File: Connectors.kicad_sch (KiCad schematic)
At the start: 13 parts, among them J2 ZX-PZ2.54-1-5PZZ, J3 Conn_01x03_Socket, U7 TJA1051T/3

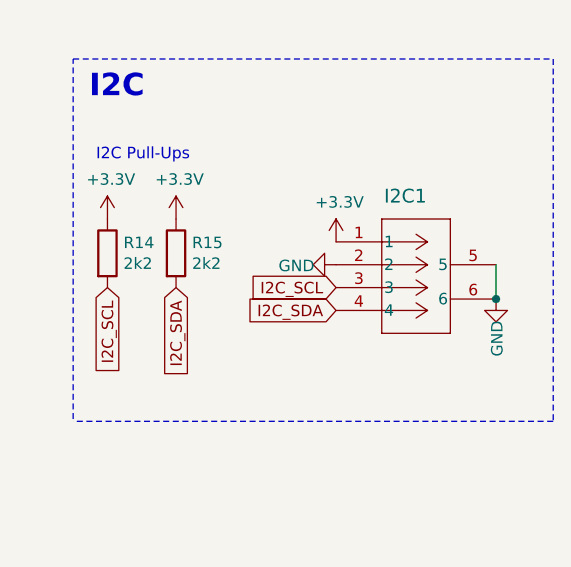
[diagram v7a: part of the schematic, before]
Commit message: IMU_IMU V1.0 is ready.
correct ch340e
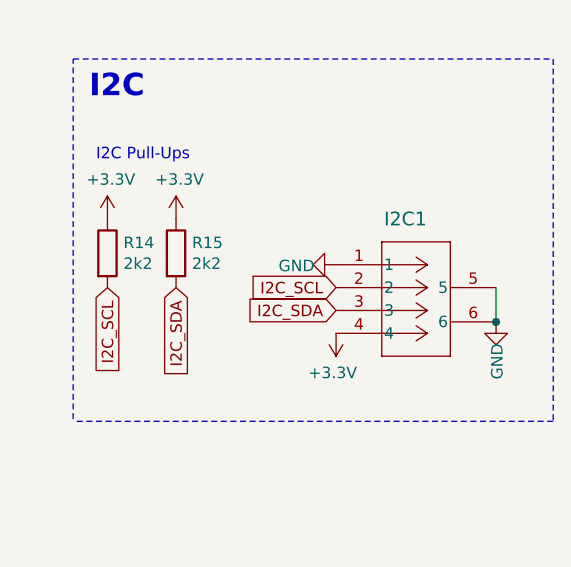
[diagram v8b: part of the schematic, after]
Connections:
- net +3.3V: now also I2C1.4; no longer I2C1.1
- net GND: now also I2C1.1; no longer I2C1.2
- net I2C_SCL: now also I2C1.2; no longer I2C1.3
- net I2C_SDA: now also I2C1.3; no longer I2C1.4
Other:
- moved on the sheet: I2C1
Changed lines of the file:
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@@
-	)
-	(junction
-		(at 218.44 67.31)
-		(diameter 0)
-		(color 0 0 0 0)
 	)
 	(junction
@@
 		(color 0 0 0 0)
 	)
+	(junction
+		(at 218.44 69.85)
+		(diameter 0)
+		(color 0 0 0 0)
+	)
 	(wire
 		(pts
@@
 		)
 	)
+	(polyline
+		(pts
+			(xy 224.79 40.64) (xy 224.79 80.899)
+		)
+		(stroke
+			(width 0)
+			(type dash)
+		)
+	)
 	(wire
 		(pts
@@
 		)
 	)
-	(wire
-		(pts
-			(xy 218.44 63.5) (xy 218.44 67.31)
-		)
-		(stroke
-			(width 0)
-			(type default)
-		)
-	)
 	(polyline
 		(pts
-			(xy 224.79 40.64) (xy 224.79 80.899)
+			(xy 224.79 80.899) (xy 171.45 80.899)
 		)
 		(stroke
@@
 	(polyline
 		(pts
-			(xy 224.79 80.899) (xy 171.45 80.899)
+			(xy 34.29 96.52) (xy 34.29 25.4)
 		)
 		(stroke
@@
 	(polyline
 		(pts
-			(xy 34.29 96.52) (xy 34.29 25.4)
+			(xy 88.9 165.989) (xy 35.56 165.989)
 		)
 		(stroke
@@
 		)
 	)
+	(wire
+		(pts
+			(xy 95.25 63.5) (xy 101.6 63.5)
+		)
+		(stroke
+			(width 0)
+			(type default)
+		)
+	)
 	(polyline
 		(pts
-			(xy 88.9 165.989) (xy 35.56 165.989)
+			(xy 171.45 80.645) (xy 171.45 40.64)
 		)
 		(stroke
@@
 	(wire
 		(pts
-			(xy 95.25 63.5) (xy 101.6 63.5)
+			(xy 60.96 138.43) (xy 62.23 138.43)
+		)
+		(stroke
+			(width 0)
+			(type default)
+		)
+	)
+	(wire
+		(pts
+			(xy 67.31 138.43) (xy 69.85 138.43)
+		)
+		(stroke
+			(width 0)
+			(type default)
+		)
+	)
+	(wire
+		(pts
+			(xy 101.6 68.58) (xy 109.22 68.58)
+		)
+		(stroke
+			(width 0)
+			(type default)
+		)
+	)
+	(wire
+		(pts
+			(xy 109.22 66.04) (xy 85.09 66.04)
+		)
+		(stroke
+			(width 0)
+			(type default)
+		)
+	)
+	(wire
+		(pts
+			(xy 101.6 63.5) (xy 101.6 68.58)
 		)
 		(stroke
@@
 	(polyline
 		(pts
-			(xy 171.45 80.645) (xy 171.45 40.64)
+			(xy 34.29 24.1301) (xy 138.43 24.1301)
 		)
 		(stroke
@@
 	(wire
 		(pts
-			(xy 60.96 138.43) (xy 62.23 138.43)
-		)
-		(stroke
-			(width 0)
-			(type default)
-		)
-	)
-	(wire
-		(pts
-			(xy 67.31 138.43) (xy 69.85 138.43)
-		)
-		(stroke
-			(width 0)
-			(type default)
-		)
-	)
-	(wire
-		(pts
-			(xy 101.6 68.58) (xy 109.22 68.58)
-		)
-		(stroke
-			(width 0)
-			(type default)
-		)
-	)
-	(wire
-		(pts
-			(xy 109.22 66.04) (xy 85.09 66.04)
-		)
-		(stroke
-			(width 0)
-			(type default)
-		)
-	)
-	(wire
-		(pts
-			(xy 101.6 63.5) (xy 101.6 68.58)
+			(xy 48.26 63.5) (xy 49.53 63.5)
 		)
 		(stroke
@@
 	(polyline
 		(pts
-			(xy 34.29 24.1301) (xy 138.43 24.1301)
+			(xy 35.56 132.08) (xy 88.9 132.08)
 		)
 		(stroke
@@
 	(wire
 		(pts
-			(xy 48.26 63.5) (xy 49.53 63.5)
-		)
-		(stroke
-			(width 0)
-			(type default)
-		)
-	)
-	(polyline
-		(pts
-			(xy 35.56 132.08) (xy 88.9 132.08)
-		)
-		(stroke
-			(width 0)
-			(type dash)
-		)
-	)
-	(wire
-		(pts
 			(xy 48.26 60.96) (xy 49.53 60.96)
 		)
@@
 		(pts
 			(xy 63.5 146.05) (xy 69.85 146.05)
+		)
+		(stroke
+			(width 0)
+			(type default)
+		)
+	)
+	(wire
+		(pts
+			(xy 218.44 66.04) (xy 218.44 69.85)
 		)
 		(stroke
@@
 	)
 	(symbol
-		(lib_id "power:+3.3V")
-		(at 200.66 60.96 0)
-		(unit 1)
-		(exclude_from_sim no)
-		(in_bom yes)
-		(on_board yes)
-		(dnp no)
-		(property "Reference" "#PWR058"
-			(at 200.66 64.77 0)
-			(effects
-				(font
-					(size 1.27 1.27)
-				)
-				(hide yes)
-			)
-		)
-		(property "Value" "+3.3V"
-			(at 201.041 56.5658 0)
-			(effects
-				(font
-					(size 1.27 1.27)
-				)
-			)
-		)
-		(property "Footprint" ""
-			(at 200.66 60.96 0)
-			(effects
-				(font
-					(size 1.27 1.27)
-				)
-				(hide yes)
-			)
-		)
-		(property "Datasheet" ""
-			(at 200.66 60.96 0)
-			(effects
-				(font
-					(size 1.27 1.27)
-				)
-				(hide yes)
-			)
-		)
-		(property "Description" ""
-			(at 200.66 60.96 0)
-			(effects
-				(font
-					(size 1.27 1.27)
-				)
-			)
-		)
-		(pin "1"
-		)
-		(instances
-			(project "MX_IMU"
-				(path "/8ed38441-7d4e-4e89-870f-07e11c6dce38/3e6b1080-2480-49a7-8bae-2dbfae5f98f5"
-					(reference "#PWR058")
-					(unit 1)
-				)
-			)
-		)
-	)
-	(symbol
 		(lib_id "power:+3V3")
 		(at 40.64 68.58 90)
@@
 	(symbol
 		(lib_id "power:GND")
-		(at 218.44 67.31 0)
+		(at 218.44 69.85 0)
 		(unit 1)
 		(exclude_from_sim no)
@@
 		(dnp no)
 		(property "Reference" "#PWR060"
-			(at 218.44 73.66 0)
+			(at 218.44 76.2 0)
 			(effects
 				(font
@@
 		)
 		(property "Value" "GND"
-			(at 218.567 71.7042 90)
+			(at 218.567 74.2442 90)
 			(effects
 				(font
@@
 		)
 		(property "Footprint" ""
-			(at 218.44 67.31 0)
+			(at 218.44 69.85 0)
 			(effects
 				(font
@@
 		)
 		(property "Datasheet" ""
-			(at 218.44 67.31 0)
+			(at 218.44 69.85 0)
 			(effects
 				(font
@@
 		)
 		(property "Description" "Power symbol creates a global label with name \"GND\" , ground"
-			(at 218.44 67.31 0)
+			(at 218.44 69.85 0)
 			(effects
 				(font
@@
 		(on_board yes)
 		(dnp no)
-		(property "Reference" "#PWR059"
+		(property "Reference" "#PWR058"
 			(at 194.31 63.5 0)
 			(effects
@@
 			(project "MX_IMU"
 				(path "/8ed38441-7d4e-4e89-870f-07e11c6dce38/3e6b1080-2480-49a7-8bae-2dbfae5f98f5"
-					(reference "#PWR059")
+					(reference "#PWR058")
 					(unit 1)
 				)
@@
 	)
 	(symbol
+		(lib_id "power:+3V3")
+		(at 200.66 71.12 180)
+		(unit 1)
+		(exclude_from_sim no)
+		(in_bom yes)
+		(on_board yes)
+		(dnp no)
+		(property "Reference" "#PWR059"
+			(at 200.66 67.31 0)
+			(effects
+				(font
+					(size 1.27 1.27)
+				)
+				(hide yes)
+			)
+		)
+		(property "Value" "+3.3V"
+			(at 200.279 75.5142 0)
+			(effects
+				(font
+					(size 1.27 1.27)
+				)
+			)
+		)
+		(property "Footprint" ""
+			(at 200.66 71.12 0)
+			(effects
+				(font
+					(size 1.27 1.27)
+				)
+				(hide yes)
+			)
+		)
+		(property "Datasheet" ""
+			(at 200.66 71.12 0)
+			(effects
+				(font
+					(size 1.27 1.27)
+				)
+				(hide yes)
+			)
+		)
+		(property "Description" ""
+			(at 200.66 71.12 0)
+			(effects
+				(font
+					(size 1.27 1.27)
+				)
+			)
+		)
+		(pin "1"
+		)
+		(instances
+			(project "MX_IMU"
+				(path "/8ed38441-7d4e-4e89-870f-07e11c6dce38/3e6b1080-2480-49a7-8bae-2dbfae5f98f5"
+					(reference "#PWR059")
+					(unit 1)
+				)
+			)
+		)
+	)
+	(symbol
 		(lib_id "SM04B-GHS-TB:SM04B-GHS-TB")
-		(at 200.66 60.96 0)
+		(at 200.66 63.5 0)
 		(unit 1)
 		(exclude_from_sim no)
@@
 		(dnp no)
 		(property "Reference" "I2C1"
-			(at 205.994 55.88 0)
+			(at 205.994 58.42 0)
 			(effects
 				(font
@@
 		)
 		(property "Value" "SM04B-GHS-TB(LF)(SN)"
-			(at 214.63 66.0399 0)
+			(at 214.63 68.5799 0)
 			(effects
 				(font
@@
 		)
 		(property "Footprint" "mylib:CONN_SM04B-GHS-TB_JST"
-			(at 200.66 60.96 0)
+			(at 200.66 63.5 0)
 			(effects
 				(font
@@
 		)
 		(property "Datasheet" "SM04B-GHS-TB"
-			(at 200.66 60.96 0)
+			(at 200.66 63.5 0)
 			(effects
 				(font
@@
 		)
 		(property "Description" ""
-			(at 200.66 60.96 0)
-			(effects
-				(font
+			(at 200.66 63.5 0)
+			(effects
+				(font
